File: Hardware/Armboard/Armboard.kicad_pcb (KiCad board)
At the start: 2 copper layers, 125.5 x 100.8 mm, 117 parts, among them J1 Test_Point, SW1 SW_Push, SW2 SW_Push, SW3 SW_Push, SW4 SW_Push, SW5 SW_Push, SW6 SW_Push, U1 OKI, U2 TM4C129E_Launchpad

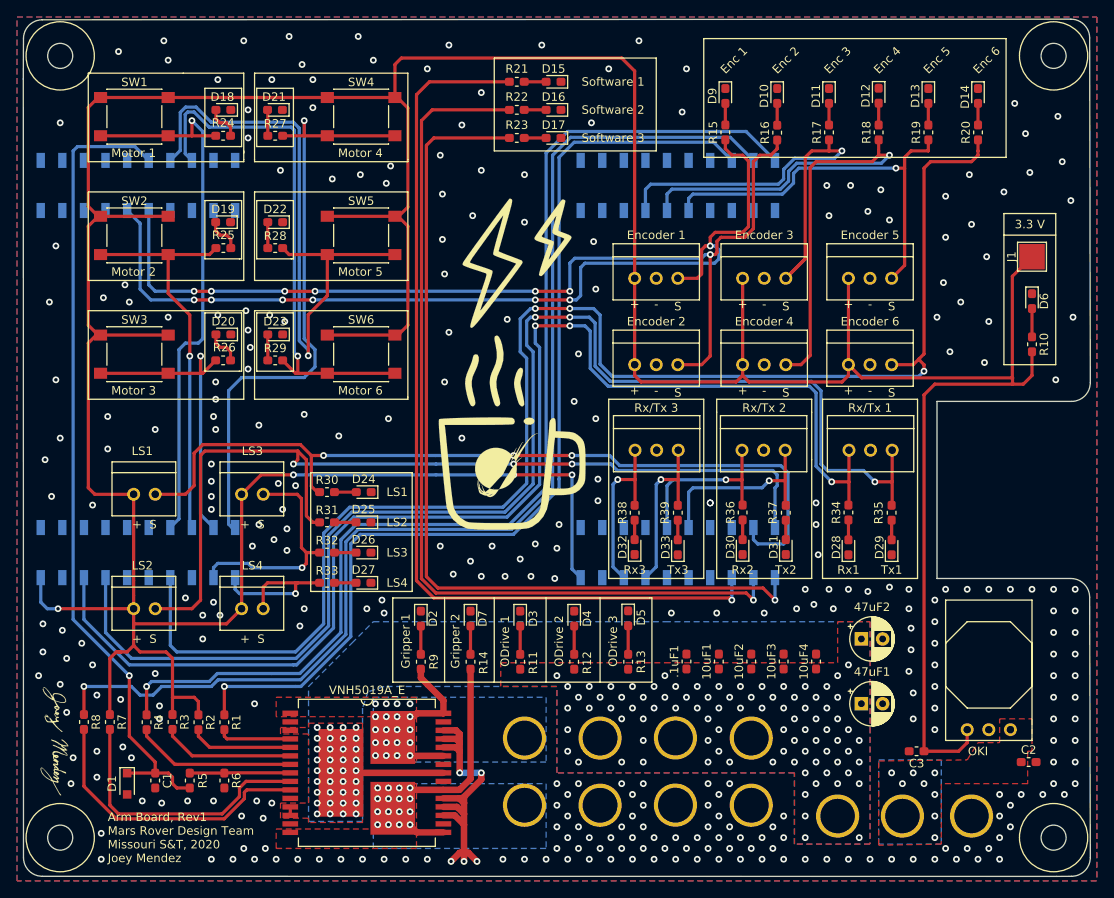
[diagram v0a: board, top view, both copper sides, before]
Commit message: moved some labels around, added rx/tx pin labels
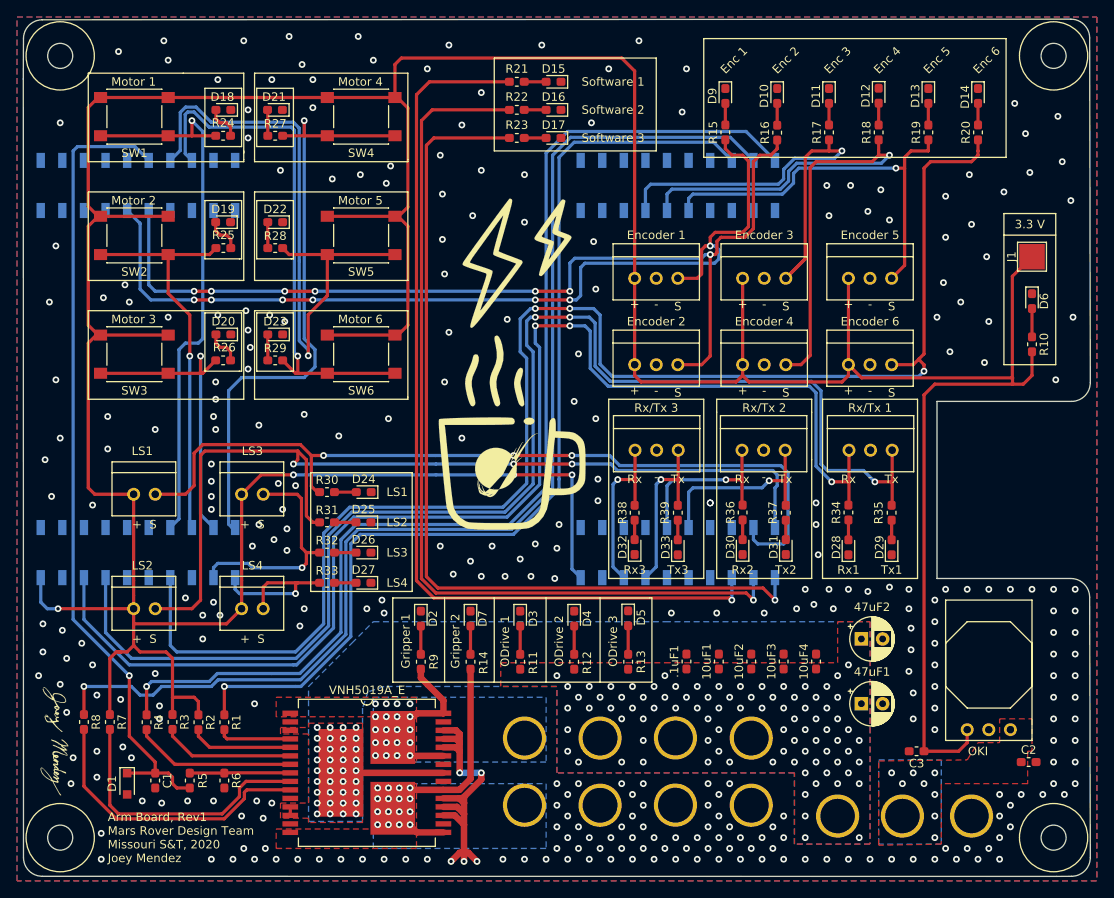
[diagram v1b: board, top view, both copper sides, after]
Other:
- board text added: "Rx"
- board text added: "Tx"

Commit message: Fixed some library issues and moved Gerbs to Manufacturing folder
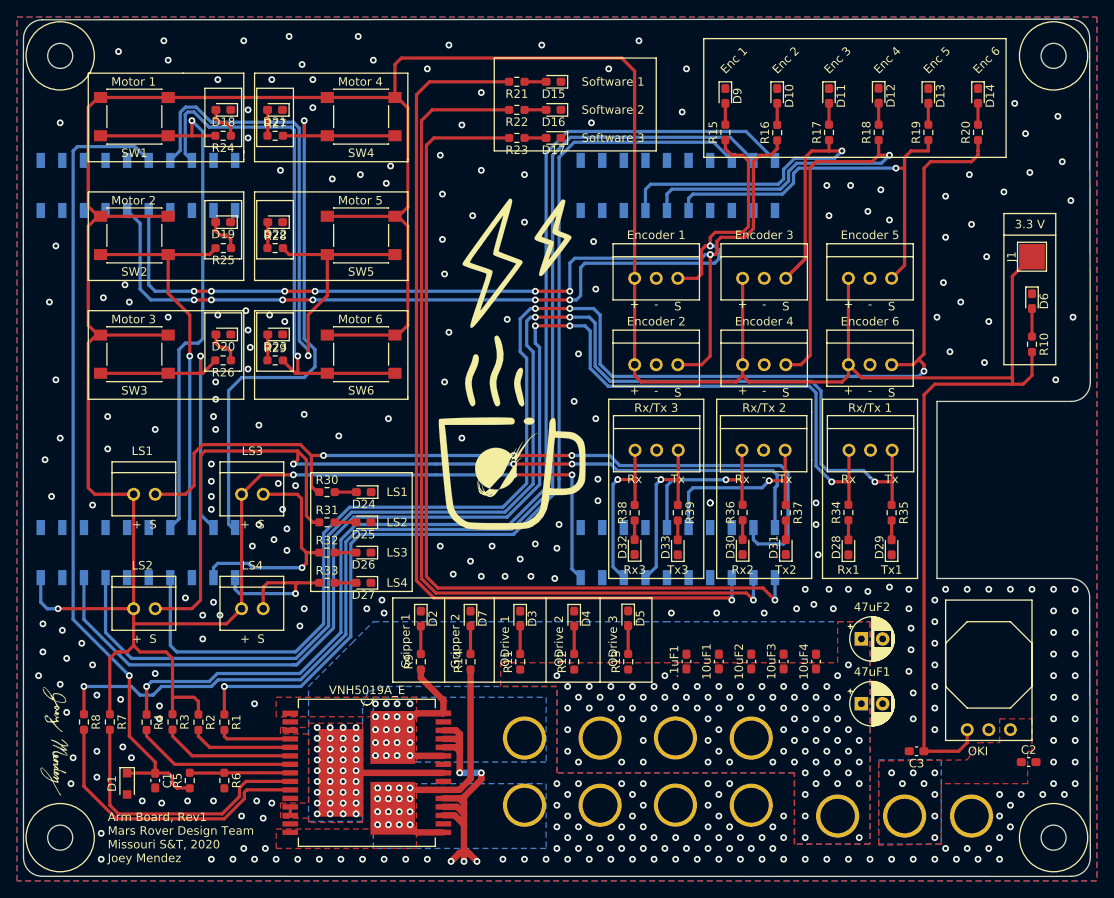
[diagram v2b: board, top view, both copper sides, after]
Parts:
- .1uF1, 10uF1, 10uF2, 10uF3, 10uF4, C1, C2, C3: footprint Capacitor_SMD:C_0603_1608Metric_Pad1.05x0.95mm_HandSolder -> Capacitor_SMD:C_0603_1608Metric_Pad1.08x0.95mm_HandSolder
- D10, D11, D12, D13, D14, D15, D16, D17, D18, D19, D2, D20, D21, D22, D23, D24, D25, D26, D27, D28, D29, D3, D30, D31, D32, D33, D4, D5, D6, D7, D9: footprint LED_SMD:LED_0603_1608Metric_Pad1.05x0.95mm_HandSolder -> Diode_SMD:D_0603_1608Metric_Pad1.05x0.95mm_HandSolder
- R1, R10, R11, R12, R13, R14, R15, R16, R17, R18, R19, R2, R20, R21, R22, R23, R24, R25, R26, R27, R28, R29, R3, R30, R31, R32, R33, R34, R35, R36, R37, R38, R39, R4, R5, R6, R7, R8, R9: footprint Resistor_SMD:R_0603_1608Metric_Pad1.05x0.95mm_HandSolder -> Resistor_SMD:R_0603_1608Metric_Pad0.98x0.95mm_HandSolder
